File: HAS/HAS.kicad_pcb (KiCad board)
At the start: 2 copper layers, 64 x 64 mm, 3 parts

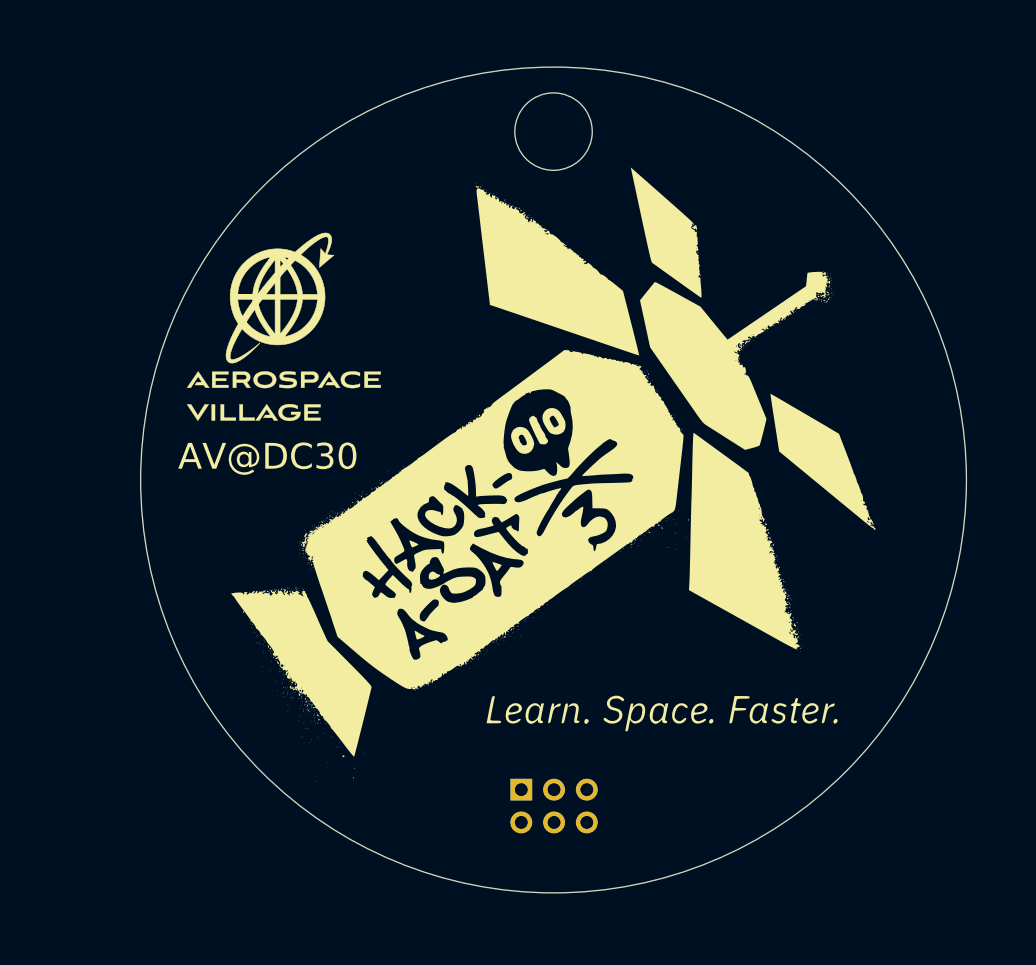
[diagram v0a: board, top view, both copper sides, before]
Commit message: updated HAS SAO with an LED
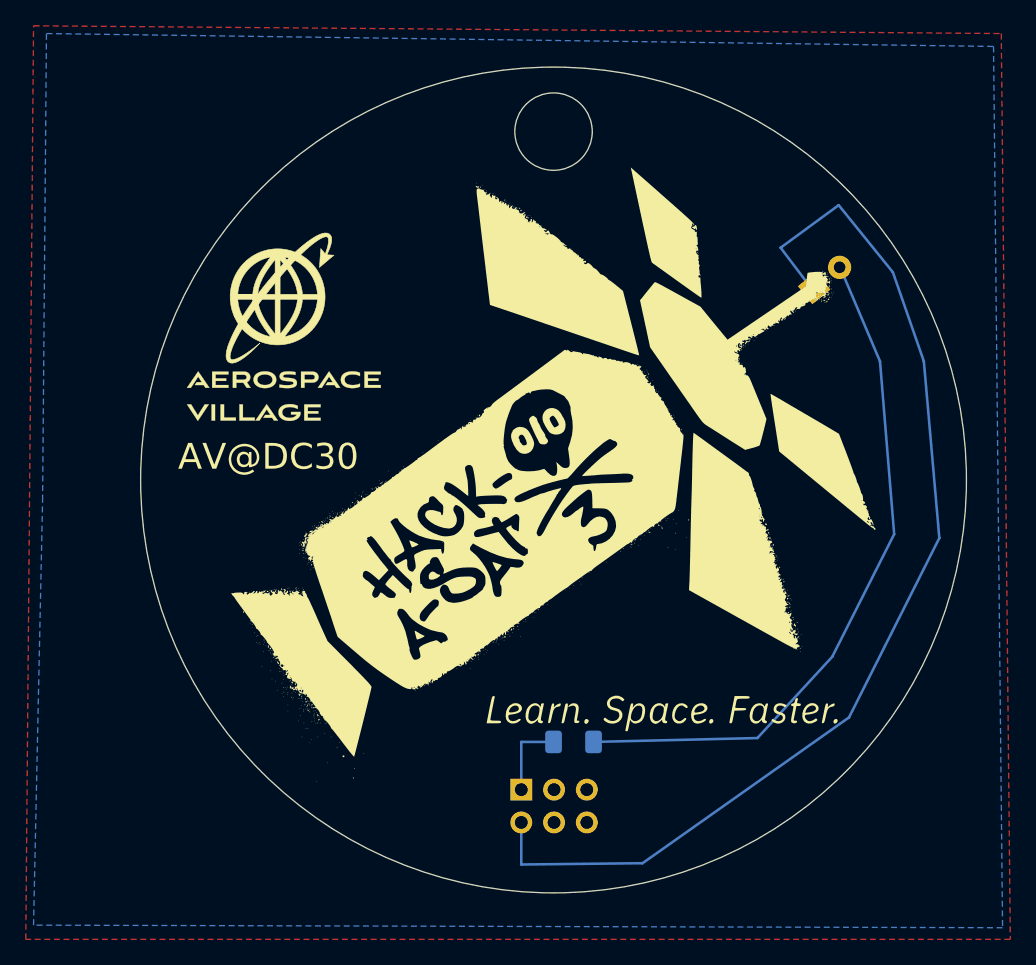
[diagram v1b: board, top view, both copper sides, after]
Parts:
- added REF**: LED_D5.0mm, LED_THT:LED_D5.0mm, F.Cu at (180.2, 85.1)
- added REF**: R_1206_3216Metric_Pad1.30x1.75mm_HandSolder, Resistor_SMD:R_1206_3216Metric_Pad1.30x1.75mm_HandSolder, B.Cu at (161.6, 120.3)
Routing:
- added copper zone on B.Cu, net (none)
- added copper zone on F.Cu, net (none)
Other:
- board text added: "v2"
- board text removed: "v1"
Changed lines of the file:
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@@
-(kicad_pcb (version 20220427) (generator pcbnew)
+(kicad_pcb (version 20220621) (generator pcbnew)
   (general
     (thickness 1.6)
@@
       (disableapertmacros false)
       (usegerberextensions true)
-      (usegerberattributes false)
-      (usegerberadvancedattributes true)
+      (usegerberattributes true)
+      (usegerberadvancedattributes false)
       (creategerberjobfile false)
       (dashed_line_dash_ratio 12.000000)
@@
   )
   (net 0 "")
+  (footprint "LED_THT:LED_D5.0mm" (layer "F.Cu")
+    (at 180.195935 85.116327 39)
+    (descr "LED, diameter 5.0mm, 2 pins, http://cdn-reichelt.de/documents/datenblatt/A500/LL-504BC2E-009.pdf")
+    (tags "LED diameter 5.0mm 2 pins")
+    (attr through_hole)
+    (fp_text reference "REF**" (at 1.27 -3.96 39) (layer "F.SilkS") hide
+        (effects (font (size 1 1) (thickness 0.15)))
+    )
+    (fp_text value "LED_D5.0mm" (at 1.27 3.96 39) (layer "F.Fab")
+        (effects (font (size 1 1) (thickness 0.15)))
+    )
+    (fp_text user "${REFERENCE}" (at 1.25 0 39) (layer "F.Fab")
+        (effects (font (size 0.8 0.8) (thickness 0.2)))
+    )
+    (fp_line (start -1.95 -3.25) (end -1.95 3.25)
+      (stroke (width 0.05) (type solid)) (layer "F.CrtYd"))
+    (fp_line (start -1.95 3.25) (end 4.5 3.25)
+      (stroke (width 0.05) (type solid)) (layer "F.CrtYd"))
+    (fp_line (start 4.5 -3.25) (end -1.95 -3.25)
+      (stroke (width 0.05) (type solid)) (layer "F.CrtYd"))
+    (fp_line (start 4.5 3.25) (end 4.5 -3.25)
+      (stroke (width 0.05) (type solid)) (layer "F.CrtYd"))
+    (pad "1" thru_hole rect (at 0 0 39) (size 1.8 1.8) (drill 0.9) (layers *.Cu *.Mask))
+    (pad "2" thru_hole circle (at 2.54 0 39) (size 1.8 1.8) (drill 0.9) (layers *.Cu *.Mask))
+    (model "${KICAD6_3DMODEL_DIR}/LED_THT.3dshapes/LED_D5.0mm.wrl"
+      (offset (xyz 0 0 0))
+      (scale (xyz 1 1 1))
+      (rotate (xyz 0 0 0))
+    )
+  )
   (footprint "LOGO" (layer "F.Cu")
     (at 160 100)
@@
     )
   )
+  (footprint "Resistor_SMD:R_1206_3216Metric_Pad1.30x1.75mm_HandSolder" (layer "B.Cu")
+    (at 161.55 120.3)
+    (descr "Resistor SMD 1206 (3216 Metric), square (rectangular) end terminal, IPC_7351 nominal with elongated pad for handsoldering. (Body size source: IPC-SM-782 page 72, https://www.pcb-3d.com/wordpress/wp-content/uploads/ipc-sm-782a_amendment_1_and_2.pdf), generated with kicad-footprint-generator")
+    (tags "resistor handsolder")
+    (attr smd)
+    (fp_text reference "REF**" (at 0 1.82) (layer "B.SilkS") hide
+        (effects (font (size 1 1) (thickness 0.15)) (justify mirror))
+    )
+    (fp_text value "R_1206_3216Metric_Pad1.30x1.75mm_HandSolder" (at 0 -1.82) (layer "B.Fab")
+        (effects (font (size 1 1) (thickness 0.15)) (justify mirror))
+    )
+    (fp_text user "${REFERENCE}" (at 0 0) (layer "B.Fab")
+        (effects (font (size 0.8 0.8) (thickness 0.12)) (justify mirror))
+    )
+    (fp_line (start -0.727064 -0.91) (end 0.727064 -0.91)
+      (stroke (width 0.12) (type solid)) (layer "B.SilkS"))
+    (fp_line (start -0.727064 0.91) (end 0.727064 0.91)
+      (stroke (width 0.12) (type solid)) (layer "B.SilkS"))
+    (fp_line (start -2.45 -1.12) (end -2.45 1.12)
+      (stroke (width 0.05) (type solid)) (layer "B.CrtYd"))
+    (fp_line (start -2.45 1.12) (end 2.45 1.12)
+      (stroke (width 0.05) (type solid)) (layer "B.CrtYd"))
+    (fp_line (start 2.45 -1.12) (end -2.45 -1.12)
+      (stroke (width 0.05) (type solid)) (layer "B.CrtYd"))
+    (fp_line (start 2.45 1.12) (end 2.45 -1.12)
+      (stroke (width 0.05) (type solid)) (layer "B.CrtYd"))
+    (fp_line (start -1.6 -0.8) (end -1.6 0.8)
+      (stroke (width 0.1) (type solid)) (layer "B.Fab"))
+    (fp_line (start -1.6 0.8) (end 1.6 0.8)
+      (stroke (width 0.1) (type solid)) (layer "B.Fab"))
+    (fp_line (start 1.6 -0.8) (end -1.6 -0.8)
+      (stroke (width 0.1) (type solid)) (layer "B.Fab"))
+    (fp_line (start 1.6 0.8) (end 1.6 -0.8)
+      (stroke (width 0.1) (type solid)) (layer "B.Fab"))
+    (pad "1" smd roundrect (at -1.55 0) (size 1.3 1.75) (layers "B.Cu" "B.Paste" "B.Mask") (roundrect_rratio 0.1923076923))
+    (pad "2" smd roundrect (at 1.55 0) (size 1.3 1.75) (layers "B.Cu" "B.Paste" "B.Mask") (roundrect_rratio 0.1923076923))
+    (model "${KICAD6_3DMODEL_DIR}/Resistor_SMD.3dshapes/R_1206_3216Metric.wrl"
+      (offset (xyz 0 0 0))
+      (scale (xyz 1 1 1))
+      (rotate (xyz 0 0 0))
+    )
+  )
+  (gr_line (start 175.8 120) (end 181.6 113.7)
+    (stroke (width 0.2) (type default)) (layer "B.Cu"))
+  (gr_line (start 182.9 118.4) (end 166.9 129.7)
+    (stroke (width 0.2) (type default)) (layer "B.Cu"))
+  (gr_line (start 185.3 90.8) (end 182.2 83.5)
+    (stroke (width 0.2) (type default)) (layer "B.Cu"))
+  (gr_line (start 186.4 104.2) (end 185.3 90.8)
+    (stroke (width 0.2) (type default)) (layer "B.Cu"))
+  (gr_line (start 189.9 104.5) (end 188.7 90.8)
+    (stroke (width 0.2) (type default)) (layer "B.Cu"))
+  (gr_line (start 188.7 90.8) (end 186.3 83.9)
+    (stroke (width 0.2) (type default)) (layer "B.Cu"))
+  (gr_line (start 163.1 120.3) (end 175.8 120)
+    (stroke (width 0.2) (type default)) (layer "B.Cu"))
+  (gr_line (start 157.5 129.8) (end 157.5 126.5)
+    (stroke (width 0.2) (type default)) (layer "B.Cu"))
+  (gr_line (start 177.6 82) (end 180.1 85.3)
+    (stroke (width 0.2) (type default)) (layer "B.Cu"))
+  (gr_line (start 157.5 124) (end 157.5 120.3)
+    (stroke (width 0.2) (type default)) (layer "B.Cu"))
+  (gr_line (start 181.6 113.7) (end 186.4 104.2)
+    (stroke (width 0.2) (type default)) (layer "B.Cu"))
+  (gr_line (start 182.9 118.4) (end 189.9 104.5)
+    (stroke (width 0.2) (type default)) (layer "B.Cu"))
+  (gr_line (start 186.3 83.9) (end 182.1 78.7)
+    (stroke (width 0.2) (type default)) (layer "B.Cu"))
+  (gr_line (start 157.5 120.3) (end 160.1 120.3)
+    (stroke (width 0.2) (type default)) (layer "B.Cu"))
+  (gr_line (start 166.9 129.7) (end 157.5 129.8)
+    (stroke (width 0.2) (type default)) (layer "B.Cu"))
+  (gr_line (start 182.1 78.7) (end 177.6 82)
+    (stroke (width 0.2) (type default)) (layer "B.Cu"))
   (gr_poly
     (pts
@@
     (effects (font (size 2 2) (thickness 0.15)))
   )
-  (gr_text "v1" (at 159.8 120.9) (layer "B.SilkS")
+  (gr_text "v2" (at 160 113.5) (layer "B.SilkS")
     (effects (font (size 1 1) (thickness 0.15)) (justify mirror))
   )
@@
     (effects (font (size 2 2) (thickness 0.15)))
   )
+  (zone (net 0) (net_name "") (layer "F.Cu") (hatch edge 0.508)
+    (connect_pads (clearance 0.508))
+    (min_thickness 0.254) (filled_areas_thickness no)
+    (fill yes (thermal_gap 0.508) (thermal_bridge_width 0.508) (island_removal_mode 2) (island_area_min 10))
+    (polygon
+      (pts
+        (xy 194.7 65.4)
+        (xy 195.4 135.6)
+        (xy 119.1 135.6)
+        (xy 119.7 64.8)
+      )
+    )
+  )
+  (zone (net 0) (net_name "") (layer "B.Cu") (hatch edge 0.508)
+    (connect_pads (clearance 0.508))
+    (min_thickness 0.254) (filled_areas_thickness no)
+    (fill yes (thermal_gap 0.508) (thermal_bridge_width 0.508) (island_removal_mode 2) (island_area_min 10))
+    (polygon
+      (pts
+        (xy 194.1 66.4)
+        (xy 194.8 134.7)
+        (xy 119.7 134.5)
+        (xy 120.4 101.6)
+        (xy 120.7 65.4)
+      )
+    )
+  )
   (group "" (id 99286be7-e8ef-4205-9d8a-9e3304bde268)

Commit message: v3 of HAS SAO
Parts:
- removed the G*** at (160.0, 100.0)
- moved REF** 7.66 mm to (157.5, 113.8), turned to 90 degrees
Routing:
- net (no net): track 0.00 -> 114.9 mm
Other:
- outline, holes or cut-outs redrawn
- board text added: "v3"
- board text removed: "v2"
